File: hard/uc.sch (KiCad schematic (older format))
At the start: 2 parts

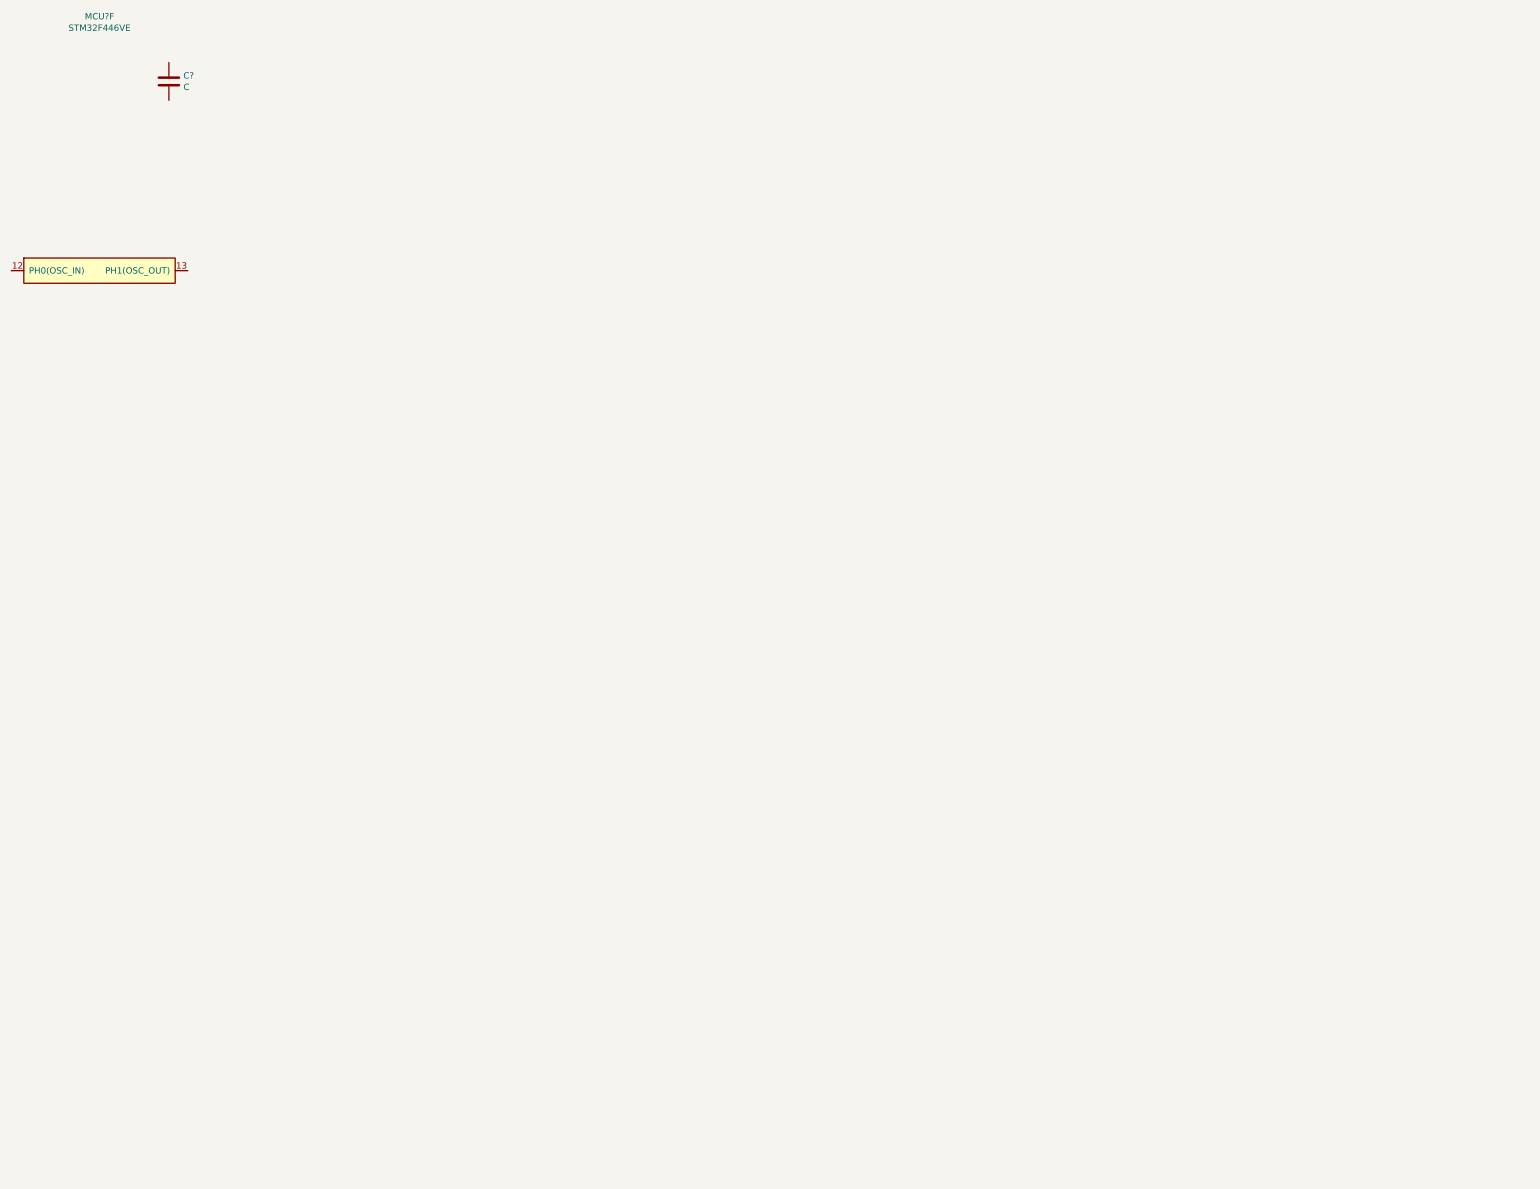
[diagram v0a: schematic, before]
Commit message: added various devices
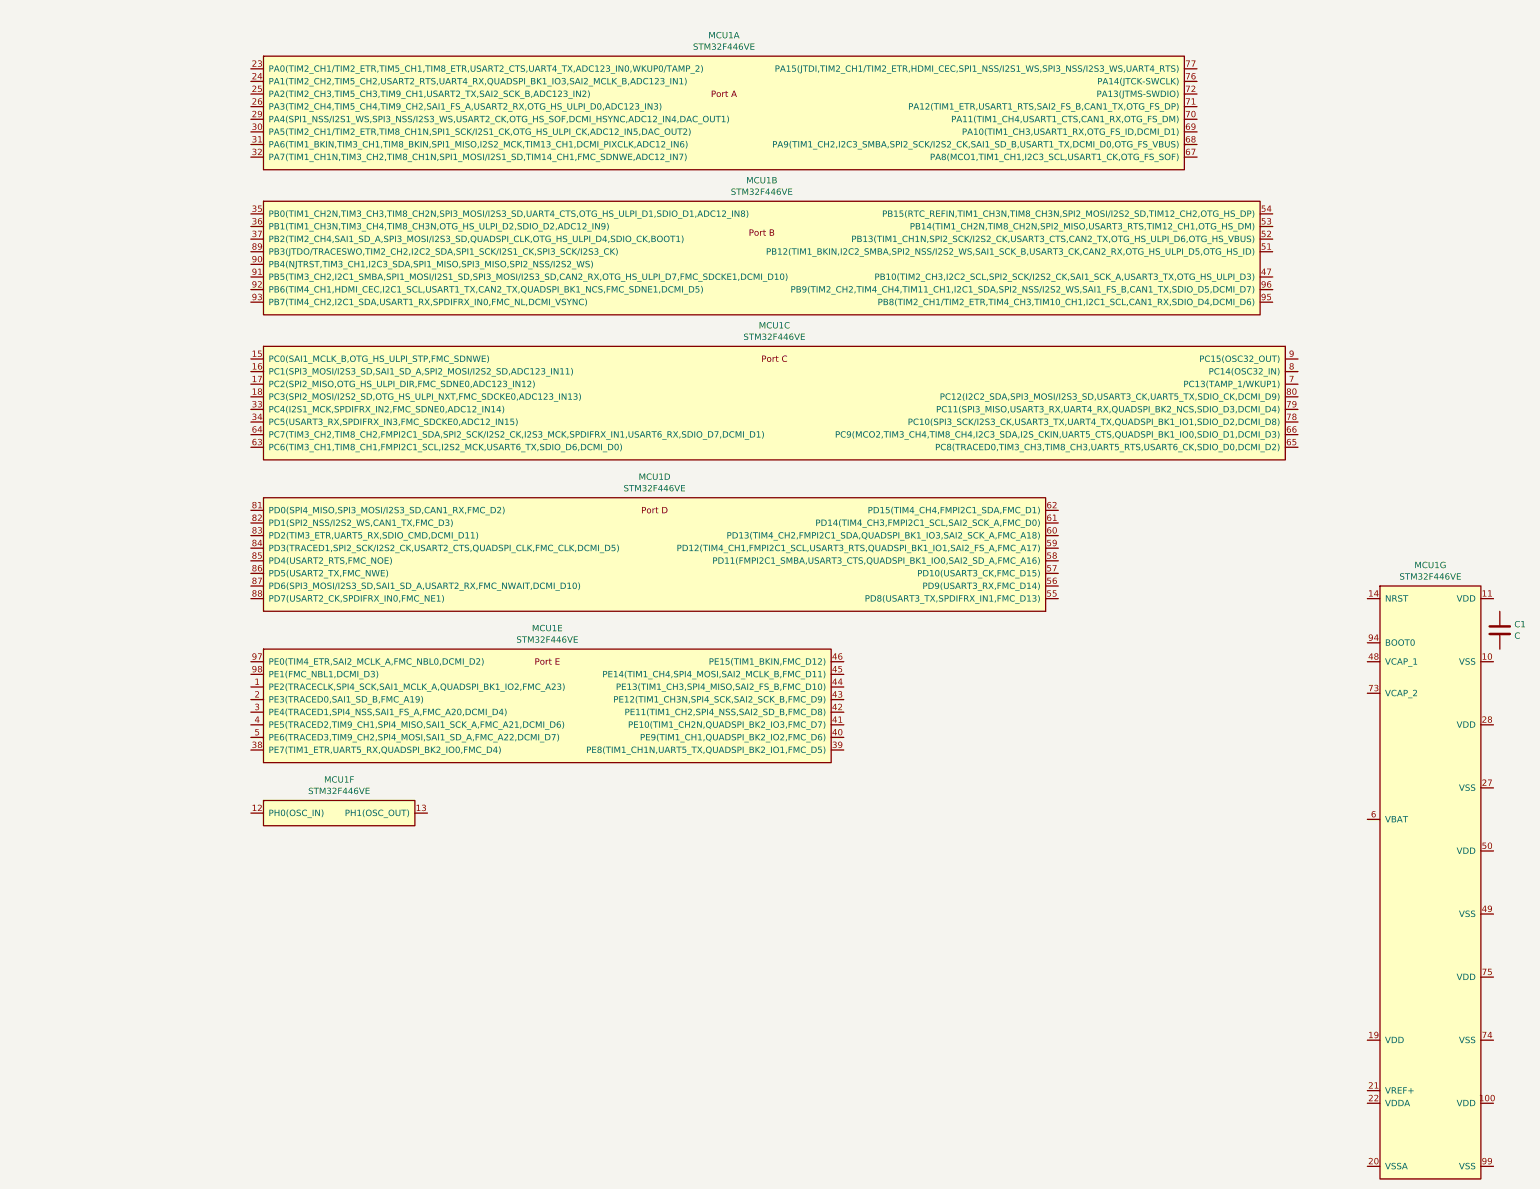
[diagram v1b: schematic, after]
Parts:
- removed MCU?: STM32F446VE, symbol led_matrix:STM32F446VE
- added MCU1: STM32F446VE, symbol led_matrix:STM32F446VE
- gave numbers to parts that had none: 1
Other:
- moved on the sheet: C1
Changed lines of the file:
@@
 $EndDescr
 $Comp
-L Device:C C?
+L Device:C C1
 U 1 1 60557FA3
-P 3600 1450
-F 0 "C?" H 3485 1496 50  0000 R CNN
-F 1 "C" H 3485 1405 50  0000 R CNN
-F 2 "" H 3638 1300 50  0001 C CNN
-F 3 "~" H 3600 1450 50  0001 C CNN
-	1    3600 1450
+P 14150 5800
+F 0 "C1" H 14035 5846 50  0000 R CNN
+F 1 "C" H 14035 5755 50  0000 R CNN
+F 2 "" H 14188 5650 50  0001 C CNN
+F 3 "~" H 14150 5800 50  0001 C CNN
+	1    14150 5800
 	-1   0    0    -1
 $EndComp
 $Comp
-L led_matrix:STM32F446VE MCU?
-U 6 1 6055A3E5
-P 3050 2850
-F 0 "MCU?" H 3050 4765 50  0000 C CNN
-F 1 "STM32F446VE" H 3050 4674 50  0000 C CNN
-F 2 "" H 3500 3650 50  0001 C CNN
-F 3 "" H 3500 3650 50  0001 C CNN
-	6    3050 2850
+L led_matrix:STM32F446VE MCU1
+U 1 1 6059CDEC
+P 8000 1250
+F 0 "MCU1" H 8000 1415 50  0000 C CNN
+F 1 "STM32F446VE" H 8000 1324 50  0000 C CNN
+F 2 "" H 8550 1600 50  0001 C CNN
+F 3 "https://www.st.com/resource/en/datasheet/stm32f446ve.pdf" H 8550 1600 50  0001 C CNN
+F 4 "C91929" H 8000 1250 50  0001 C CNN "JLCPCB_Part_Number"
+F 5 "STMicroelectronics" H 8000 1250 50  0001 C CNN "MF"
+F 6 "STM32F446VET6" H 8000 1250 50  0001 C CNN "MPN"
+F 7 "ST MICROELECTRONICS LQFP-100_14X14X05P ROHS" H 8000 1250 50  0001 C CNN "Description"
+	1    8000 1250
 	1    0    0    -1
 $EndComp
+$Comp
+L led_matrix:STM32F446VE MCU1
+U 2 1 605A0D1E
+P 8300 2400
+F 0 "MCU1" H 8300 2565 50  0000 C CNN
+F 1 "STM32F446VE" H 8300 2474 50  0000 C CNN
+F 2 "" H 8850 2750 50  0001 C CNN
+F 3 "https://www.st.com/resource/en/datasheet/stm32f446ve.pdf" H 8850 2750 50  0001 C CNN
+F 4 "C91929" H 8300 2400 50  0001 C CNN "JLCPCB_Part_Number"
+F 5 "STMicroelectronics" H 8300 2400 50  0001 C CNN "MF"
+F 6 "STM32F446VET6" H 8300 2400 50  0001 C CNN "MPN"
+F 7 "ST MICROELECTRONICS LQFP-100_14X14X05P ROHS" H 8300 2400 50  0001 C CNN "Description"
+	2    8300 2400
+	1    0    0    -1
+$EndComp
+$Comp
+L led_matrix:STM32F446VE MCU1
+U 3 1 605A8D95
+P 8400 3550
+F 0 "MCU1" H 8400 3715 50  0000 C CNN
+F 1 "STM32F446VE" H 8400 3624 50  0000 C CNN
+F 2 "" H 8950 3900 50  0001 C CNN
+F 3 "https://www.st.com/resource/en/datasheet/stm32f446ve.pdf" H 8950 3900 50  0001 C CNN
+F 4 "C91929" H 8400 3550 50  0001 C CNN "JLCPCB_Part_Number"
+F 5 "STMicroelectronics" H 8400 3550 50  0001 C CNN "MF"
+F 6 "STM32F446VET6" H 8400 3550 50  0001 C CNN "MPN"
+F 7 "ST MICROELECTRONICS LQFP-100_14X14X05P ROHS" H 8400 3550 50  0001 C CNN "Description"
+	3    8400 3550
+	1    0    0    -1
+$EndComp
+$Comp
+L led_matrix:STM32F446VE MCU1
+U 4 1 605AC720
+P 7450 4750
+F 0 "MCU1" H 7450 4915 50  0000 C CNN
+F 1 "STM32F446VE" H 7450 4824 50  0000 C CNN
+F 2 "Package_QFP:LQFP-100_14x14mm_P0.5mm" H 8000 5100 50  0001 C CNN
+F 3 "https://www.st.com/resource/en/datasheet/stm32f446ve.pdf" H 8000 5100 50  0001 C CNN
+F 4 "C91929" H 7450 4750 50  0001 C CNN "JLCPCB_Part_Number"
+F 5 "STMicroelectronics" H 7450 4750 50  0001 C CNN "MF"
+F 6 "STM32F446VET6" H 7450 4750 50  0001 C CNN "MPN"
+F 7 "ST MICROELECTRONICS LQFP-100_14X14X05P ROHS" H 7450 4750 50  0001 C CNN "Description"
+F 8 "497-15375-ND" H 7450 4750 50  0001 C CNN "DigiKey_Part_Number"
+	4    7450 4750
+	1    0    0    -1
+$EndComp
+$Comp
+L led_matrix:STM32F446VE MCU1
+U 5 1 605B01CA
+P 6600 5950
+F 0 "MCU1" H 6600 6115 50  0000 C CNN
+F 1 "STM32F446VE" H 6600 6024 50  0000 C CNN
+F 2 "" H 7150 6300 50  0001 C CNN
+F 3 "https://www.st.com/resource/en/datasheet/stm32f446ve.pdf" H 7150 6300 50  0001 C CNN
+F 4 "C91929" H 6600 5950 50  0001 C CNN "JLCPCB_Part_Number"
+F 5 "STMicroelectronics" H 6600 5950 50  0001 C CNN "MF"
+F 6 "STM32F446VET6" H 6600 5950 50  0001 C CNN "MPN"
+F 7 "ST MICROELECTRONICS LQFP-100_14X14X05P ROHS" H 6600 5950 50  0001 C CNN "Description"
+	5    6600 5950
+	1    0    0    -1
+$EndComp
+$Comp
+L led_matrix:STM32F446VE MCU1
+U 6 1 605B418A
+P 4950 7150
+F 0 "MCU1" H 4950 7315 50  0000 C CNN
+F 1 "STM32F446VE" H 4950 7224 50  0000 C CNN
+F 2 "" H 5500 7500 50  0001 C CNN
+F 3 "https://www.st.com/resource/en/datasheet/stm32f446ve.pdf" H 5500 7500 50  0001 C CNN
+F 4 "C91929" H 4950 7150 50  0001 C CNN "JLCPCB_Part_Number"
+F 5 "STMicroelectronics" H 4950 7150 50  0001 C CNN "MF"
+F 6 "STM32F446VET6" H 4950 7150 50  0001 C CNN "MPN"
+F 7 "ST MICROELECTRONICS LQFP-100_14X14X05P ROHS" H 4950 7150 50  0001 C CNN "Description"
+	6    4950 7150
+	1    0    0    -1
+$EndComp
+$Comp
+L led_matrix:STM32F446VE MCU1
+U 7 1 605B81AB
+P 13600 5450
+F 0 "MCU1" H 13600 5615 50  0000 C CNN
+F 1 "STM32F446VE" H 13600 5524 50  0000 C CNN
+F 2 "" H 14150 5800 50  0001 C CNN
+F 3 "https://www.st.com/resource/en/datasheet/stm32f446ve.pdf" H 14150 5800 50  0001 C CNN
+F 4 "C91929" H 13600 5450 50  0001 C CNN "JLCPCB_Part_Number"
+F 5 "STMicroelectronics" H 13600 5450 50  0001 C CNN "MF"
+F 6 "STM32F446VET6" H 13600 5450 50  0001 C CNN "MPN"
+F 7 "ST MICROELECTRONICS LQFP-100_14X14X05P ROHS" H 13600 5450 50  0001 C CNN "Description"
+	7    13600 5450
+	1    0    0    -1
+$EndComp

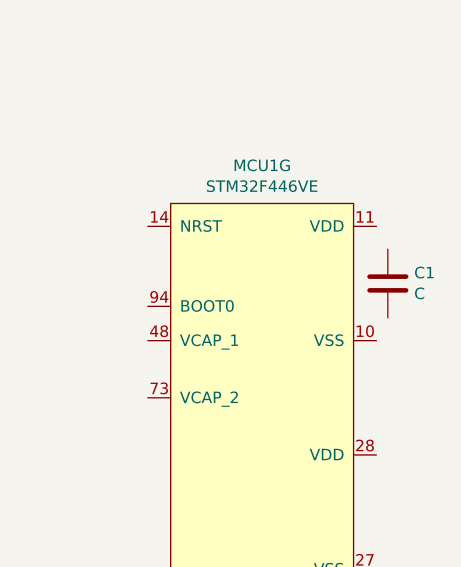
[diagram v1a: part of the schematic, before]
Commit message: added usb connector
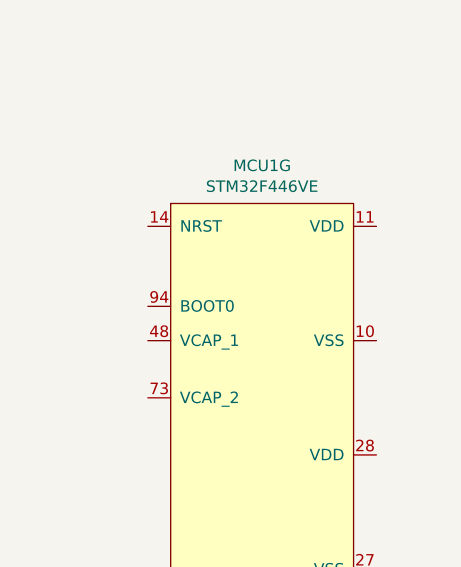
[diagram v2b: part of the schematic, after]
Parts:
- removed C1: C, symbol Device:C
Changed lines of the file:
@@
 $EndDescr
-$Comp
-L Device:C C1
-U 1 1 60557FA3
-P 14150 5800
-F 0 "C1" H 14035 5846 50  0000 R CNN
-F 1 "C" H 14035 5755 50  0000 R CNN
-F 2 "" H 14188 5650 50  0001 C CNN
-F 3 "~" H 14150 5800 50  0001 C CNN
-	1    14150 5800
-	-1   0    0    -1
-$EndComp
 $Comp
 L led_matrix:STM32F446VE MCU1
